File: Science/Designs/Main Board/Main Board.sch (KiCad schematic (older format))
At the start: 89 parts, among them J1 I2C_OUT, J10 AIR_SENS, J11 MOISTURE_SENS, J12 LIMIT3, J13 LIMIT2, J14 LIMIT1, J15 SERVO3, J16 SERVO2, J17 SERVO1, J18 MOTOR1_SIG, J19 MOTOR2_SIG, J2 ANE_SENS, J20 MOTOR3_SIG, J4 ENCODER2, J5 ENCODER1, J7 ATMO_SENS, P1 LS7366R, P2 LS7366R, P3 RPI_HEADER, P4 PWR_IN, P5 UV_SENS, P6 DIST_SENS, P7 I2C_TEST, P8 THERMO_SENS, P9 SPI_TEST, U1 SN74HC14N, U2 TLV2544ID, U3 PCA9685, U4 PCA9685, U5 ACPL-064L-500E, U6 ACPL-064L-500E, U7 LM317T, Y1 20MHz, Y2 20MHz

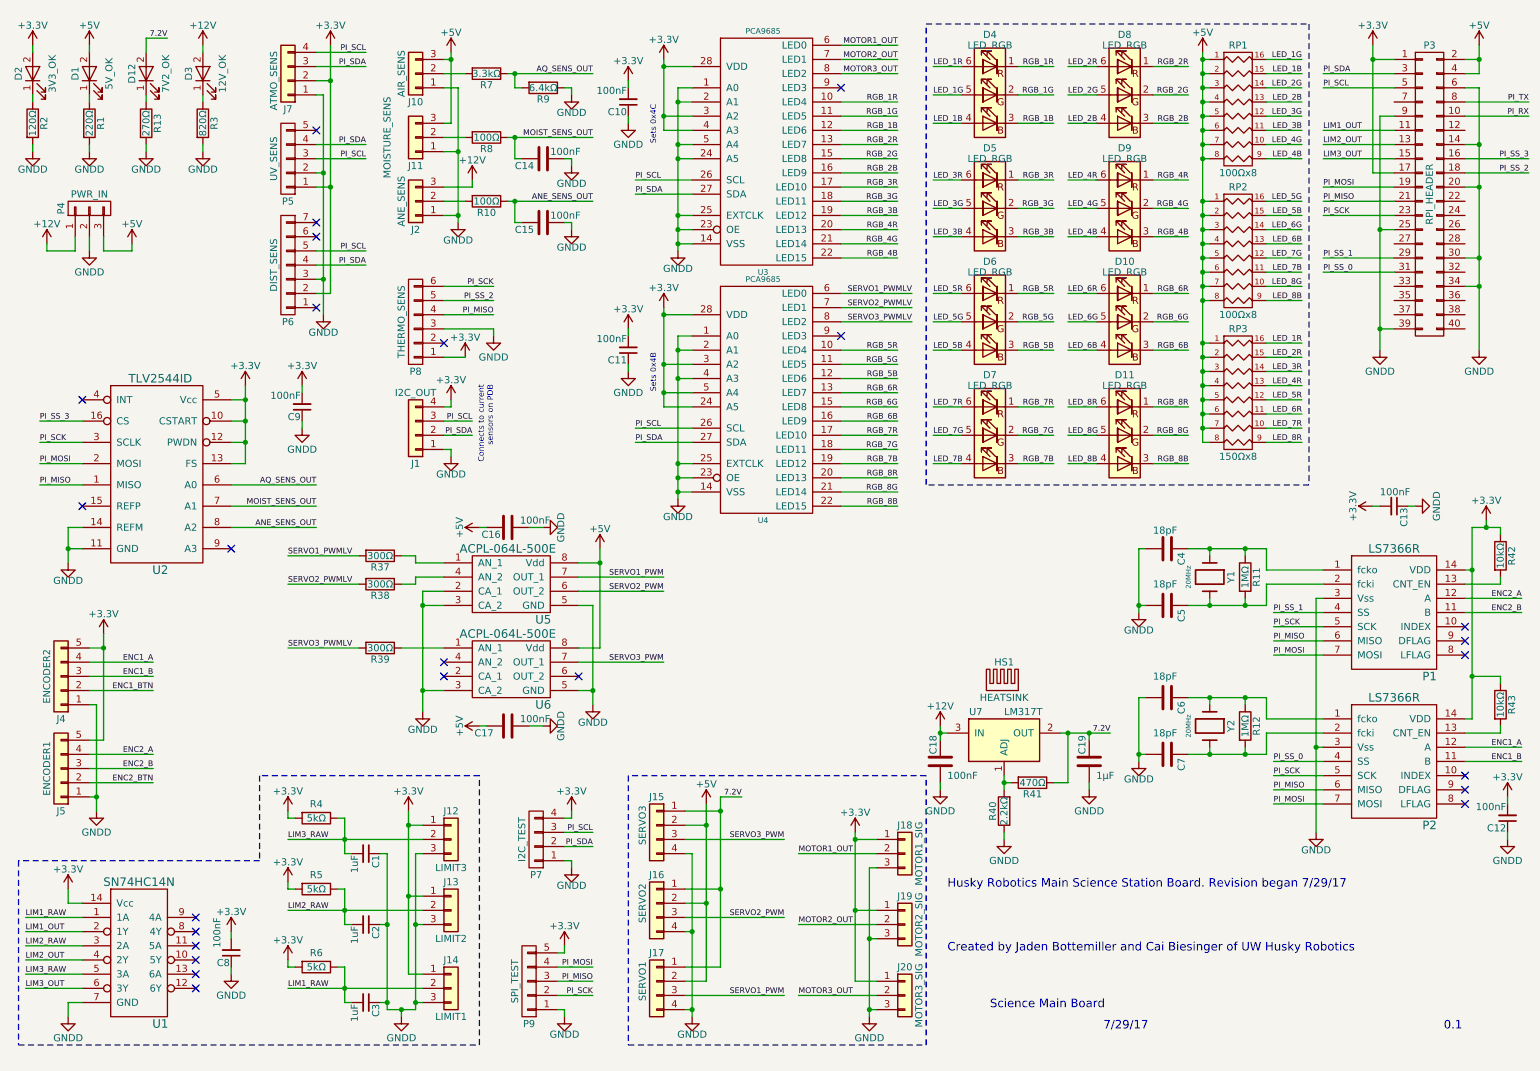
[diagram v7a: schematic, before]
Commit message: Very close to finished main board
Just needs ground plane work now!
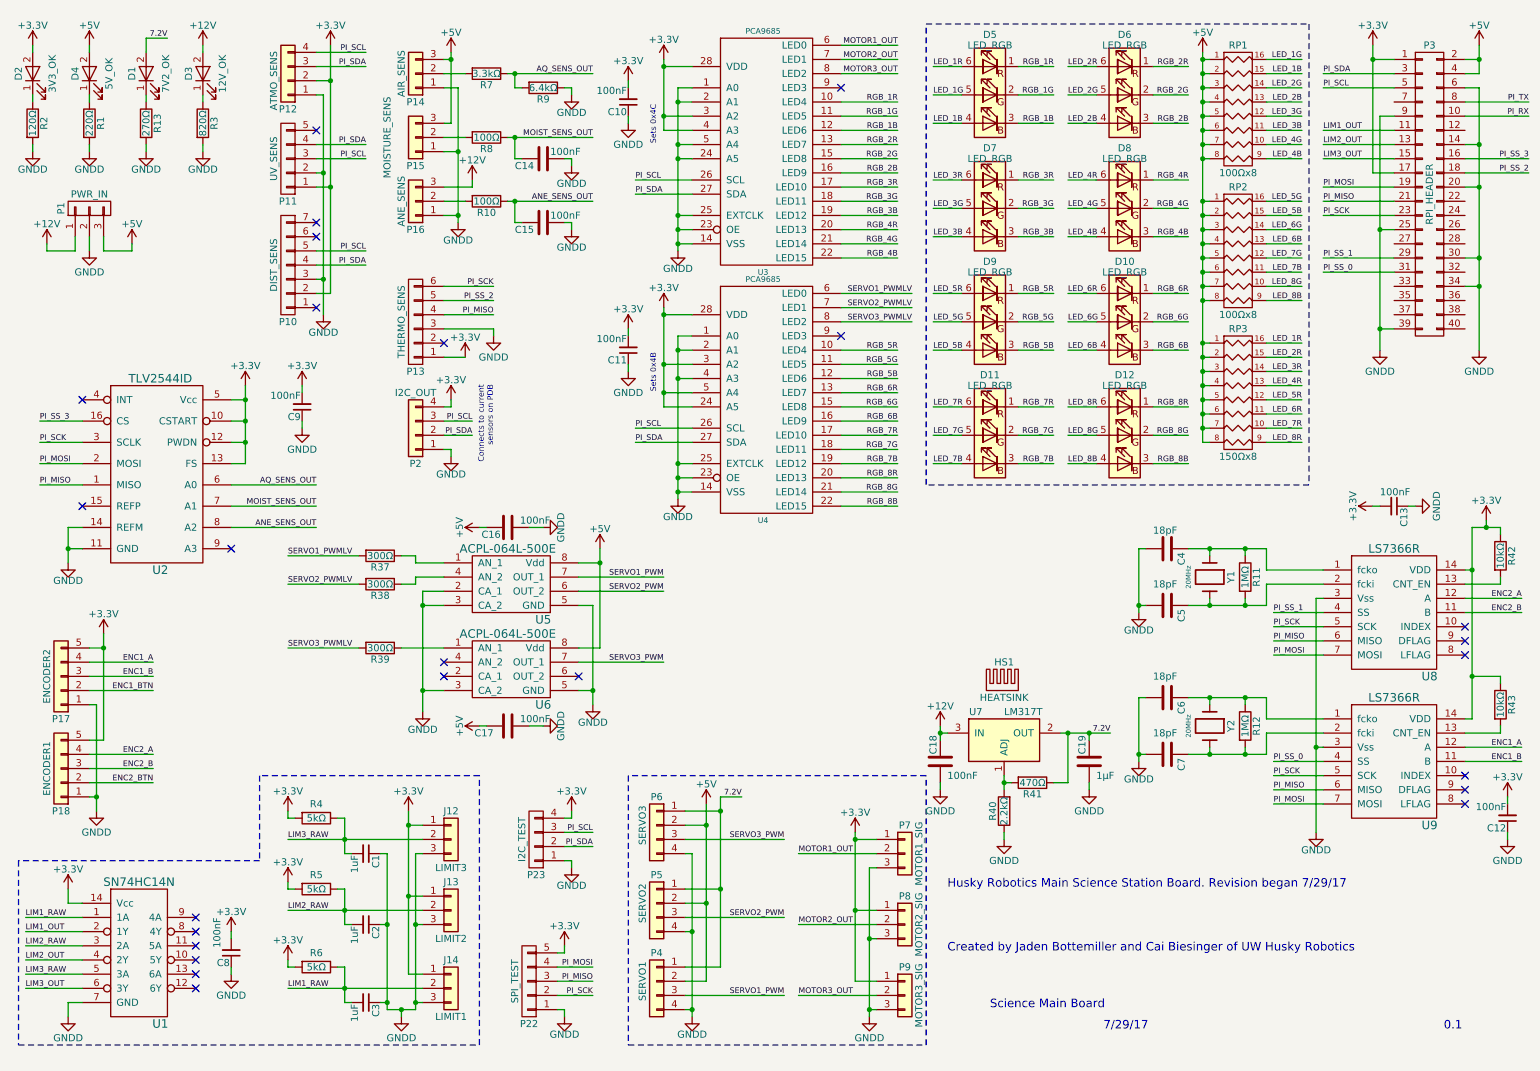
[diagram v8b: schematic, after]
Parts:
- renumbered D12 to D1, D7 to D11, D11 to D12, D1 to D4, D4 to D5, D8 to D6, D5 to D7, D9 to D8, D6 to D9, P4 to P1, P6 to P10, P5 to P11, J7 to P12, P8 to P13, J10 to P14, J11 to P15, J2 to P16, J4 to P17, J5 to P18, J1 to P2, P9 to P22, P7 to P23, J17 to P4, J16 to P5, J15 to P6, J18 to P7, J19 to P8, J20 to P9, P1 to U8, P2 to U9
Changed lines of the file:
@@
 $EndComp
 $Comp
-L LED-RESCUE-Main_Board D1
+L LED-RESCUE-Main_Board D4
 U 1 1 5A23588B
 P 1000 900
-F 0 "D1" H 1000 1000 50  0000 C CNN
+F 0 "D4" H 1000 1000 50  0000 C CNN
 F 1 "5V_OK" H 1000 761 50  0000 C CNN
 F 2 "LEDs:LED_D5.0mm" H 1000 900 50  0001 C CNN
@@
 $EndComp
 $Comp
-L Conn_01x04 J16
+L Conn_01x04 P5
 U 1 1 5A23AC0D
 P 5000 6750
-F 0 "J16" H 5000 6950 50  0000 C CNN
+F 0 "P5" H 5000 6950 50  0000 C CNN
 F 1 "SERVO2" V 5100 6750 50  0000 C CNN
 F 2 "ScienceFootprints:MOLEX_22-23-2041" H 5000 6750 50  0001 C CNN
@@
 $EndComp
 $Comp
-L Conn_01x04 J17
+L Conn_01x04 P4
 U 1 1 5A23AC72
 P 5000 7300
-F 0 "J17" H 5000 7500 50  0000 C CNN
+F 0 "P4" H 5000 7500 50  0000 C CNN
 F 1 "SERVO1" V 5100 7300 50  0000 C CNN
 F 2 "ScienceFootprints:MOLEX_22-23-2041" H 5000 7300 50  0001 C CNN
@@
 $EndComp
 $Comp
-L Conn_01x04 J15
+L Conn_01x04 P6
 U 1 1 5A23ACDF
 P 5000 6200
-F 0 "J15" H 5000 6400 50  0000 C CNN
+F 0 "P6" H 5000 6400 50  0000 C CNN
 F 1 "SERVO3" V 5100 6200 50  0000 C CNN
 F 2 "ScienceFootprints:MOLEX_22-23-2041" H 5000 6200 50  0001 C CNN
@@
 $EndComp
 $Comp
-L Conn_01x05 J4
+L Conn_01x05 P17
 U 1 1 5A235192
 P 800 5150
-F 0 "J4" H 800 5450 50  0000 C CNN
+F 0 "P17" H 800 5450 50  0000 C CNN
 F 1 "ENCODER2" V 900 5150 50  0000 C CNN
 F 2 "ScienceFootprints:MOLEX_22-23-2051" H 800 5150 50  0001 C CNN
@@
 $EndComp
 $Comp
-L Conn_01x05 J5
+L Conn_01x05 P18
 U 1 1 5A23521B
 P 800 5800
-F 0 "J5" H 800 6100 50  0000 C CNN
+F 0 "P18" H 800 6100 50  0000 C CNN
 F 1 "ENCODER1" V 900 5800 50  0000 C CNN
 F 2 "ScienceFootprints:MOLEX_22-23-2051" H 800 5800 50  0001 C CNN
@@
 $EndComp
 $Comp
-L Conn_01x03 J18
+L Conn_01x03 P7
 U 1 1 5A2355F4
 P 6750 6400
-F 0 "J18" H 6750 6600 50  0000 C CNN
+F 0 "P7" H 6750 6600 50  0000 C CNN
 F 1 "MOTOR1_SIG" V 6850 6400 50  0000 C CNN
 F 2 "ScienceFootprints:MOLEX_22-23-2031" H 6750 6400 50  0001 C CNN
@@
 $EndComp
 $Comp
-L Conn_01x03 J19
+L Conn_01x03 P8
 U 1 1 5A2364A4
 P 6750 6900
-F 0 "J19" H 6750 7100 50  0000 C CNN
+F 0 "P8" H 6750 7100 50  0000 C CNN
 F 1 "MOTOR2_SIG" V 6850 6900 50  0000 C CNN
 F 2 "ScienceFootprints:MOLEX_22-23-2031" H 6750 6900 50  0001 C CNN
@@
 $EndComp
 $Comp
-L Conn_01x03 J20
+L Conn_01x03 P9
 U 1 1 5A236523
 P 6750 7400
-F 0 "J20" H 6750 7600 50  0000 C CNN
+F 0 "P9" H 6750 7600 50  0000 C CNN
 F 1 "MOTOR3_SIG" V 6850 7400 50  0000 C CNN
 F 2 "ScienceFootprints:MOLEX_22-23-2031" H 6750 7400 50  0001 C CNN
@@
 $EndComp
 $Comp
-L LS7366R P2
+L LS7366R U9
 U 1 1 5A2865B8
 P 10200 5750
-F 0 "P2" H 10450 5300 60  0000 C CNN
+F 0 "U9" H 10450 5300 60  0000 C CNN
 F 1 "LS7366R" H 10200 6200 60  0000 C CNN
 F 2 "Housings_SOIC:SOIC-14_3.9x8.7mm_Pitch1.27mm" H 10200 5900 60  0001 C CNN
@@
 $EndComp
 $Comp
-L LS7366R P1
+L LS7366R U8
 U 1 1 5A286788
 P 10200 4700
-F 0 "P1" H 10450 4250 60  0000 C CNN
+F 0 "U8" H 10450 4250 60  0000 C CNN
 F 1 "LS7366R" H 10200 5150 60  0000 C CNN
 F 2 "Housings_SOIC:SOIC-14_3.9x8.7mm_Pitch1.27mm" H 10200 4850 60  0001 C CNN
@@
 PI_SDA
 $Comp
-L Conn_01x04 J1
+L Conn_01x04 P2
 U 1 1 5A28ABD5
 P 3300 3450
-F 0 "J1" H 3300 3650 50  0000 C CNN
+F 0 "P2" H 3300 3650 50  0000 C CNN
 F 1 "I2C_OUT" H 3300 3150 50  0000 C CNN
 F 2 "ScienceFootprints:MOLEX_22-23-2041" H 3300 3450 50  0001 C CNN
@@
 PI_SCK
 $Comp
-L Conn_01x04 J7
+L Conn_01x04 P12
 U 1 1 5A513CAF
 P 2400 950
-F 0 "J7" H 2400 1150 50  0000 C CNN
+F 0 "P12" H 2400 1150 50  0000 C CNN
 F 1 "ATMO_SENS" V 2500 950 50  0000 C CNN
 F 2 "ScienceFootprints:MOLEX_22-23-2041" H 2400 950 50  0001 C CNN
@@
 PI_SCL
 $Comp
-L Conn_01x03 J10
+L Conn_01x03 P14
 U 1 1 5A51C34F
 P 3300 900
-F 0 "J10" H 3300 1100 50  0000 C CNN
+F 0 "P14" H 3300 1100 50  0000 C CNN
 F 1 "AIR_SENS" V 3400 900 50  0000 C CNN
 F 2 "ScienceFootprints:MOLEX_22-23-2031" H 3300 900 50  0001 C CNN
@@
 $EndComp
 $Comp
-L Conn_01x03 J11
+L Conn_01x03 P15
 U 1 1 5A51C3F1
 P 3300 1350
-F 0 "J11" H 3300 1550 50  0000 C CNN
+F 0 "P15" H 3300 1550 50  0000 C CNN
 F 1 "MOISTURE_SENS" V 3500 1350 50  0000 C CNN
 F 2 "ScienceFootprints:MOLEX_22-23-2031" H 3300 1350 50  0001 C CNN
@@
 	2500 3350 2500 3400
 $Comp
-L LED_RGB-RESCUE-Main_Board D4
+L LED_RGB-RESCUE-Main_Board D5
 U 1 1 5A5A06CE
 P 7350 1050
-F 0 "D4" H 7350 1475 50  0000 C CNN
+F 0 "D5" H 7350 1475 50  0000 C CNN
 F 1 "LED_RGB" H 7350 1400 50  0000 C CNN
 F 2 "ScienceFootprints:SLV6A-FKB" H 7350 1000 50  0001 C CNN
@@
 	7800 850  7550 850
 $Comp
-L LED_RGB-RESCUE-Main_Board D5
+L LED_RGB-RESCUE-Main_Board D7
 U 1 1 5A5ACA74
 P 7350 1850
-F 0 "D5" H 7350 2275 50  0000 C CNN
+F 0 "D7" H 7350 2275 50  0000 C CNN
 F 1 "LED_RGB" H 7350 2200 50  0000 C CNN
 F 2 "ScienceFootprints:SLV6A-FKB" H 7350 1800 50  0001 C CNN
@@
 	7800 1650 7550 1650
 $Comp
-L LED_RGB-RESCUE-Main_Board D6
+L LED_RGB-RESCUE-Main_Board D9
 U 1 1 5A5ACE36
 P 7350 2650
-F 0 "D6" H 7350 3075 50  0000 C CNN
+F 0 "D9" H 7350 3075 50  0000 C CNN
 F 1 "LED_RGB" H 7350 3000 50  0000 C CNN
 F 2 "ScienceFootprints:SLV6A-FKB" H 7350 2600 50  0001 C CNN
@@
 	7800 2450 7550 2450
 $Comp
-L LED_RGB-RESCUE-Main_Board D7
+L LED_RGB-RESCUE-Main_Board D11
 U 1 1 5A5AD0A5
 P 7350 3450
-F 0 "D7" H 7350 3875 50  0000 C CNN
+F 0 "D11" H 7350 3875 50  0000 C CNN
 F 1 "LED_RGB" H 7350 3800 50  0000 C CNN
 F 2 "ScienceFootprints:SLV6A-FKB" H 7350 3400 50  0001 C CNN
@@
 	7800 3250 7550 3250
 $Comp
-L LED_RGB-RESCUE-Main_Board D8
+L LED_RGB-RESCUE-Main_Board D6
 U 1 1 5A5ADA58
 P 8300 1050
-F 0 "D8" H 8300 1475 50  0000 C CNN
+F 0 "D6" H 8300 1475 50  0000 C CNN
 F 1 "LED_RGB" H 8300 1400 50  0000 C CNN
 F 2 "ScienceFootprints:SLV6A-FKB" H 8300 1000 50  0001 C CNN
@@
 	8750 850  8500 850
 $Comp
-L LED_RGB-RESCUE-Main_Board D9
+L LED_RGB-RESCUE-Main_Board D8
 U 1 1 5A5ADA85
 P 8300 1850
-F 0 "D9" H 8300 2275 50  0000 C CNN
+F 0 "D8" H 8300 2275 50  0000 C CNN
 F 1 "LED_RGB" H 8300 2200 50  0000 C CNN
 F 2 "ScienceFootprints:SLV6A-FKB" H 8300 1800 50  0001 C CNN
@@
 	8750 2450 8500 2450
 $Comp
-L LED_RGB-RESCUE-Main_Board D11
+L LED_RGB-RESCUE-Main_Board D12
 U 1 1 5A5ADADF
 P 8300 3450
-F 0 "D11" H 8300 3875 50  0000 C CNN
+F 0 "D12" H 8300 3875 50  0000 C CNN
 F 1 "LED_RGB" H 8300 3800 50  0000 C CNN
 F 2 "ScienceFootprints:SLV6A-FKB" H 8300 3400 50  0001 C CNN
@@
 Connects to current\nsensors on PDB
 $Comp
-L CONN_01X04 P7
+L CONN_01X04 P23
 U 1 1 5A5CD0EE
 P 4150 6300
-F 0 "P7" H 4150 6550 50  0000 C CNN
+F 0 "P23" H 4150 6550 50  0000 C CNN
 F 1 "I2C_TEST" V 4250 6300 50  0000 C CNN
 F 2 "Pin_Headers:Pin_Header_Straight_1x04_Pitch2.54mm" H 4150 6300 50  0001 C CNN
@@
 	4350 6250 4550 6250
 $Comp
-L CONN_01X05 P9
+L CONN_01X05 P22
 U 1 1 5A5CEE99
 P 4100 7300
-F 0 "P9" H 4100 7600 50  0000 C CNN
+F 0 "P22" H 4100 7600 50  0000 C CNN
 F 1 "SPI_TEST" V 4200 7300 50  0000 C CNN
 F 2 "Pin_Headers:Pin_Header_Straight_1x05_Pitch2.54mm" H 4100 7300 50  0001 C CNN
@@
 	4350 7100 4350 7050
 $Comp
-L CONN_01X05 P5
+L CONN_01X05 P11
 U 1 1 5A5D4ED2
 P 2400 1500
-F 0 "P5" H 2400 1800 50  0000 C CNN
+F 0 "P11" H 2400 1800 50  0000 C CNN
 F 1 "UV_SENS" V 2500 1500 50  0000 C CNN
 F 2 "ScienceFootprints:MOLEX_22-23-2051" H 2400 1500 50  0001 C CNN
@@
 	2950 750  2600 750
 $Comp
-L CONN_01X07 P6
+L CONN_01X07 P10
 U 1 1 5A5DA272
 P 2400 2250
-F 0 "P6" H 2400 2650 50  0000 C CNN
+F 0 "P10" H 2400 2650 50  0000 C CNN
 F 1 "DIST_SENS" V 2500 2250 50  0000 C CNN
 F 2 "ScienceFootprints:MOLEX_22-23-2071" H 2400 2250 50  0001 C CNN
@@
 $EndComp
 $Comp
-L CONN_01X06 P8
+L CONN_01X06 P13
 U 1 1 5A5ED133
 P 3300 2650
-F 0 "P8" H 3300 3000 50  0000 C CNN
+F 0 "P13" H 3300 3000 50  0000 C CNN
 F 1 "THERMO_SENS" V 3400 2650 50  0000 C CNN
 F 2 "ScienceFootprints:MOLEX_22-23-2061" H 3300 2650 50  0001 C CNN
@@
 	3500 2500 3850 2500
 $Comp
-L CONN_01X03 P4
+L CONN_01X03 P1
 U 1 1 5A606AC2
 P 1000 1850
-F 0 "P4" H 1000 2050 50  0000 C CNN
+F 0 "P1" H 1000 2050 50  0000 C CNN
 F 1 "PWR_IN" V 1100 1850 50  0000 C CNN
 F 2 "ScienceFootprints:PHOENIX_1792232" H 1000 1850 50  0001 C CNN
@@
 Connection ~ 8400 5700
 $Comp
-L Conn_01x03 J2
+L Conn_01x03 P16
 U 1 1 5A61BA7C
 P 3300 1800
-F 0 "J2" H 3300 2000 50  0000 C CNN
+F 0 "P16" H 3300 2000 50  0000 C CNN
 F 1 "ANE_SENS" V 3400 1800 50  0000 C CNN
 F 2 "ScienceFootprints:MOLEX_22-23-2031" H 3300 1800 50  0001 C CNN
@@
 LED_8R
 $Comp
-L LED-RESCUE-Main_Board D12
+L LED-RESCUE-Main_Board D1
 U 1 1 5A67395C
 P 1400 900
-F 0 "D12" H 1400 1000 50  0000 C CNN
+F 0 "D1" H 1400 1000 50  0000 C CNN
 F 1 "7V2_OK" H 1400 761 50  0000 C CNN
 F 2 "LEDs:LED_D5.0mm" H 1400 900 50  0001 C CNN
